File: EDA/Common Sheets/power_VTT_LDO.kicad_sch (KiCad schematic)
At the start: 26 parts, among them J5 Conn_01x04, U10 AZ1117-2.85, U9 TLV62569DBV

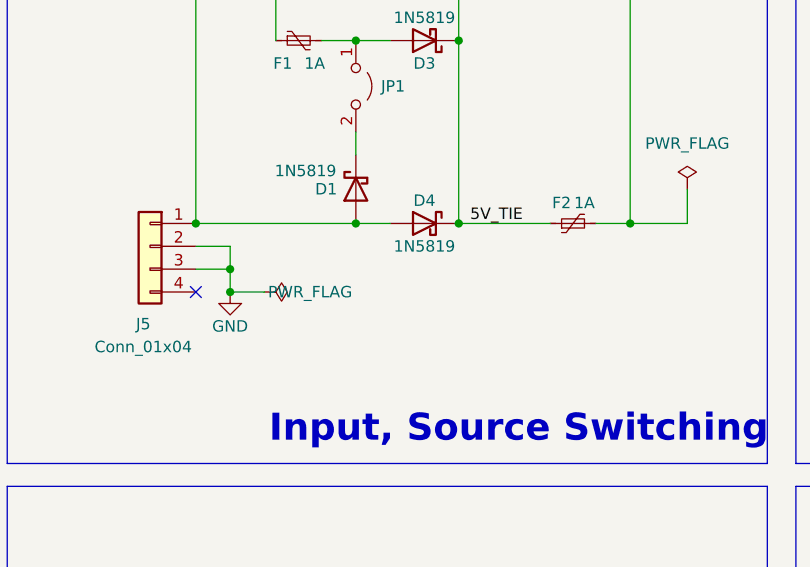
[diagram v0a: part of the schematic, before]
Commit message: Tidying up PCB footprint slightly, more work needed, ERC passes on narrow variants
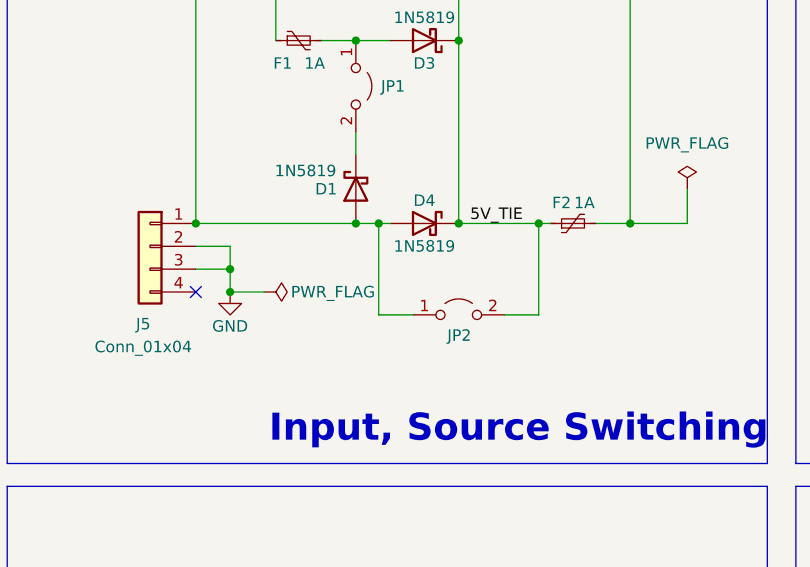
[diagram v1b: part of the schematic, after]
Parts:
- added JP2: Jumper_2_Open, Connector_PinHeader_2.54mm:PinHeader_2x01_P2.54mm_Vertical, symbol Jumper:Jumper_2_Open
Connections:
- net +5VIN: now also JP2.1 (A)
- net 5V_TIE: now also JP2.2 (B)
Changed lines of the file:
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@@
 	)
 	(junction
+		(at 80.01 66.04)
+		(diameter 0)
+		(color 0 0 0 0)
+	)
+	(junction
 		(at 73.66 116.84)
 		(diameter 0)
@@
 	)
 	(junction
+		(at 62.23 66.04)
+		(diameter 0)
+		(color 0 0 0 0)
+	)
+	(junction
 		(at 41.91 66.04)
 		(diameter 0)
@@
 	(wire
 		(pts
-			(xy 71.12 66.04) (xy 81.28 66.04)
+			(xy 71.12 66.04) (xy 80.01 66.04)
 		)
 		(stroke
@@
 	(wire
 		(pts
+			(xy 62.23 76.2) (xy 66.04 76.2)
+		)
+		(stroke
+			(width 0)
+			(type default)
+		)
+	)
+	(wire
+		(pts
 			(xy 50.8 116.84) (xy 50.8 113.03)
 		)
@@
 	(wire
 		(pts
+			(xy 76.2 76.2) (xy 80.01 76.2)
+		)
+		(stroke
+			(width 0)
+			(type default)
+		)
+	)
+	(wire
+		(pts
 			(xy 86.36 66.04) (xy 90.17 66.04)
 		)
@@
 	(wire
 		(pts
+			(xy 80.01 66.04) (xy 80.01 76.2)
+		)
+		(stroke
+			(width 0)
+			(type default)
+		)
+	)
+	(wire
+		(pts
 			(xy 59.69 30.48) (xy 59.69 34.29)
 		)
@@
 	(wire
 		(pts
-			(xy 59.69 66.04) (xy 63.5 66.04)
+			(xy 59.69 66.04) (xy 62.23 66.04)
 		)
 		(stroke
@@
 	(wire
 		(pts
+			(xy 62.23 66.04) (xy 63.5 66.04)
+		)
+		(stroke
+			(width 0)
+			(type default)
+		)
+	)
+	(wire
+		(pts
 			(xy 223.52 34.29) (xy 223.52 35.56)
 		)
@@
 	(wire
 		(pts
+			(xy 62.23 66.04) (xy 62.23 76.2)
+		)
+		(stroke
+			(width 0)
+			(type default)
+		)
+	)
+	(wire
+		(pts
 			(xy 96.52 62.23) (xy 96.52 66.04)
 		)
@@
 	(wire
 		(pts
+			(xy 80.01 66.04) (xy 81.28 66.04)
+		)
+		(stroke
+			(width 0)
+			(type default)
+		)
+	)
+	(wire
+		(pts
 			(xy 185.42 52.07) (xy 185.42 55.88)
 		)
@@
 		)
 		(property "Value" "PWR_FLAG"
-			(at 54.61 73.66 90)
+			(at 57.15 73.66 90)
 			(effects
 				(font
@@
 					(unit 1)
 				)
+			)
+		)
+	)
+	(symbol
+		(lib_id "Jumper:Jumper_2_Open")
+		(at 71.12 76.2 0)
+		(unit 1)
+		(exclude_from_sim no)
+		(in_bom yes)
+		(on_board yes)
+		(dnp no)
+		(property "Reference" "JP2"
+			(at 69.85 78.486 0)
+			(effects
+				(font
+					(size 1.27 1.27)
+				)
+				(justify left)
+			)
+		)
+		(property "Value" "Jumper_2_Open"
+			(at 71.12 73.66 90)
+			(effects
+				(font
+					(size 1.27 1.27)
+				)
+				(justify left)
+				(hide yes)
+			)
+		)
+		(property "Footprint" "Connector_PinHeader_2.54mm:PinHeader_2x01_P2.54mm_Vertical"
+			(at 71.12 76.2 0)
+			(effects
+				(font
+					(size 1.27 1.27)
+				)
+				(hide yes)
+			)
+		)
+		(property "Datasheet" "~"
+			(at 71.12 76.2 0)
+			(effects
+				(font
+					(size 1.27 1.27)
+				)
+				(hide yes)
+			)
+		)
+		(property "Description" "Jumper, 2-pole, open"
+			(at 71.12 76.2 0)
+			(effects
+				(font
+					(size 1.27 1.27)
+				)
+				(hide yes)
+			)
+		)
+		(property "LCSC" "N/A"
+			(at 71.12 76.2 0)
+			(effects
+				(font
+					(size 1.27 1.27)
+				)
+				(hide yes)
+			)
+		)
+		(property "LCSC Part #" "N/A"
+			(at 71.12 76.2 0)
+			(effects
+				(font
+					(size 1.27 1.27)
+				)
+				(hide yes)
+			)
+		)
+		(pin "1"
+		)
+		(pin "2"
+		)
+		(instances
+			(project "GBSCSI2_2.5N_Pico"
+				(path "/93ed3756-682c-4bf3-aa83-42c6b59d82c2/eb232e5c-fd69-4529-8cf9-3d8932039455"
+					(reference "JP2")
+					(unit 1)
+				)

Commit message: Resuming work
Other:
- moved on the sheet: C27, C28, C29, C30, C32, C33, C34, L2, R49, R50, R51, R52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
